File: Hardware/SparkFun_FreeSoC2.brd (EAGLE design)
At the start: 116.8 x 53.3 mm, 109 parts, among them U1 CY8C5888AXI-LP035, U2 MIC5219 5V, U3 MIC5219 3.3V, U4 2A/20V, U7 CY8C5868LTI-LP039, Y1 32.768kHz

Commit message: Revisions from QC check
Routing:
- net 5V: track 212.3 -> 214.7 mm
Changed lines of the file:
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@@
 <wire x1="54.96" y1="34.67" x2="54.96" y2="33.305" width="0.2032" layer="1"/>
 <wire x1="54.96" y1="33.305" x2="55.245" y2="33.02" width="0.2032" layer="1"/>
-<via x="55.245" y="33.02" extent="1-16" drill="0.254"/>
+<via x="55.245" y="33.02" extent="1-16" drill="0.508"/>
 <wire x1="55.245" y1="33.02" x2="59.436" y2="33.02" width="0.2032" layer="16"/>
 <wire x1="59.436" y1="33.02" x2="60.579" y2="34.163" width="0.2032" layer="16"/>
@@
 <contactref element="C9" pad="2"/>
 <wire x1="68.127" y1="33.837" x2="67.691" y2="33.401" width="0.2032" layer="1"/>
-<via x="67.691" y="33.401" extent="1-16" drill="0.254"/>
+<via x="67.691" y="33.401" extent="1-16" drill="0.508"/>
 <via x="67.691" y="17.78" extent="1-16" drill="0.254"/>
 <via x="20.447" y="37.084" extent="1-16" drill="0.254"/>
@@
 <wire x1="60.96" y1="16.891" x2="61.214" y2="16.637" width="0.2032" layer="1"/>
 <wire x1="52.563" y1="34.813" x2="52.578" y2="34.798" width="0.2032" layer="1"/>
-<via x="52.578" y="34.798" extent="1-16" drill="0.254"/>
+<via x="52.578" y="34.798" extent="1-16" drill="0.508"/>
 <wire x1="68.635" y1="19.05" x2="67.945" y2="19.05" width="0.2032" layer="1"/>
 <wire x1="67.945" y1="19.05" x2="67.691" y2="18.796" width="0.2032" layer="1"/>
@@
 <via x="14.605" y="25.781" extent="1-16" drill="0.254"/>
 <wire x1="53.34" y1="17.708" x2="53.34" y2="16.51" width="0.2032" layer="1"/>
-<via x="53.34" y="16.51" extent="1-16" drill="0.254"/>
+<via x="53.34" y="16.51" extent="1-16" drill="0.508"/>
 <wire x1="33.346" y1="37.719" x2="33.346" y2="38.68" width="0.2032" layer="1"/>
 <wire x1="33.346" y1="38.68" x2="33.401" y2="38.735" width="0.2032" layer="1"/>
@@
 <wire x1="27.051" y1="12.065" x2="27.051" y2="5.588" width="1.016" layer="16"/>
 <wire x1="27.051" y1="5.588" x2="55.499" y2="5.588" width="1.016" layer="16"/>
-<wire x1="57.404" y1="6.731" x2="58.42" y2="6.731" width="1.016" layer="16"/>
+<wire x1="56.642" y1="6.731" x2="58.42" y2="6.731" width="1.016" layer="16"/>
 <via x="58.42" y="6.731" extent="1-16" drill="0.508"/>
 <wire x1="58.42" y1="6.731" x2="58.42" y2="2.667" width="1.016" layer="1"/>
@@
 <wire x1="71.81" y1="28.829" x2="71.81" y2="29.155" width="0.2032" layer="1"/>
 <wire x1="71.81" y1="29.155" x2="71.755" y2="29.21" width="0.2032" layer="1"/>
-<wire x1="55.499" y1="5.588" x2="57.404" y2="6.731" width="0" layer="19" extent="16-16"/>
+<wire x1="56.642" y1="6.731" x2="55.499" y2="5.588" width="1.016" layer="16"/>
 </signal>
 <signal name="DEBUG_LED">

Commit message: Fixed silk/part value for target IC
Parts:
- U1: value CY8C5888AXI-LP035 -> CY8C5888AXI-LP096
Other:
- board text added: "CY8C5888AXI-LP096"
- board text removed: "CY8C5888AXI-LP035"
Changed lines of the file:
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@@
 <layer number="56" name="wert" color="7" fill="1" visible="no" active="no"/>
 <layer number="57" name="tCAD" color="7" fill="1" visible="no" active="no"/>
+<layer number="59" name="tCarbon" color="7" fill="1" visible="no" active="no"/>
+<layer number="60" name="bCarbon" color="7" fill="1" visible="no" active="no"/>
 <layer number="90" name="Modules" color="5" fill="1" visible="no" active="no"/>
 <layer number="91" name="Nets" color="2" fill="1" visible="no" active="no"/>
@@
 <layer number="127" name="_tValues" color="7" fill="1" visible="no" active="no"/>
 <layer number="128" name="_bValues" color="7" fill="1" visible="no" active="no"/>
+<layer number="129" name="Mask" color="7" fill="1" visible="no" active="no"/>
 <layer number="131" name="tAdjust" color="7" fill="1" visible="no" active="no"/>
 <layer number="132" name="bAdjust" color="7" fill="1" visible="no" active="no"/>
@@
 <text x="35.56" y="9.652" size="1.524" layer="21" font="vector" ratio="15" align="center-left">PSoC5LP
 Dev Board</text>
-<text x="54.737" y="35.814" size="0.8128" layer="21" font="vector" ratio="15">CY8C5888AXI-LP035</text>
+<text x="54.737" y="35.814" size="0.8128" layer="21" font="vector" ratio="15">CY8C5888AXI-LP096</text>
 <text x="27.813" y="26.543" size="0.8128" layer="21" font="vector" ratio="15">CY8C5868LTI-LP039</text>
 </plain>
@@
 <attribute name="DESIGNER" value="M. Hord" x="46.99" y="-27.94" size="1.778" layer="51"/>
 </element>
-<element name="U1" library="SparkFun-DigitalIC" package="TQFP-100-14X14MM" value="CY8C5888AXI-LP035" x="60.96" y="26.67">
+<element name="U1" library="SparkFun-DigitalIC" package="TQFP-100-14X14MM" value="CY8C5888AXI-LP096" x="60.96" y="26.67">
 <attribute name="PROD_ID" value="IC-12190" x="60.96" y="26.67" size="1.778" layer="27" font="vector" ratio="15" display="off"/>
 </element>

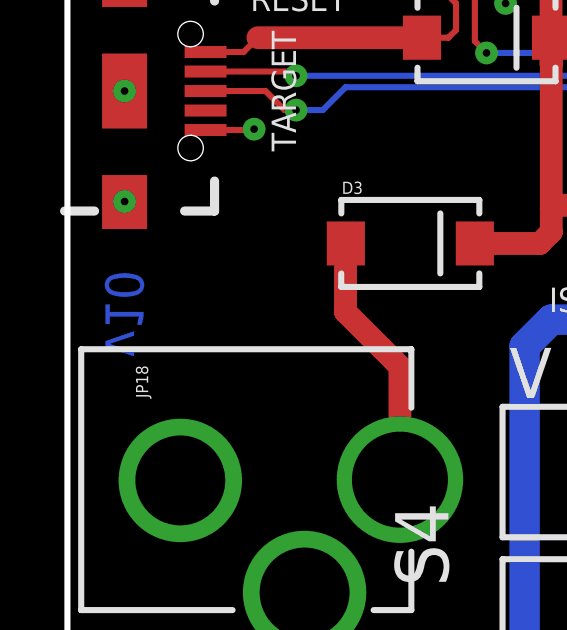
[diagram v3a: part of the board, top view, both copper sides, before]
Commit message: Rev to 11 to fix rev #, layers issue
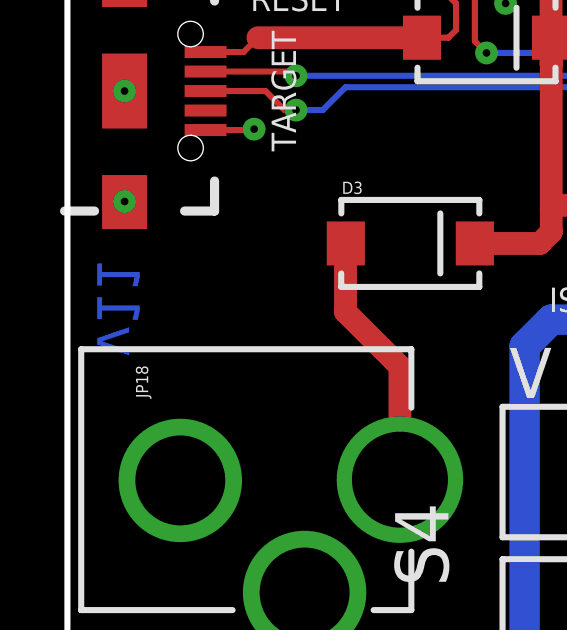
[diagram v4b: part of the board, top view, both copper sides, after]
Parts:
- added U$2: (no value), SparkFun-Aesthetics:CREATIVE_COMMONS
- FRAME1, FRAME2, FRAME3: device SparkFun-Aesthetics:CREATIVE_COMMONS -> SparkFun-Aesthetics:DUMMY
- moved FRAME1 37.8 mm to (-15.2, -15.2)
- moved FRAME2 37.4 mm to (-15.2, -16.5)
- moved FRAME3 37.0 mm to (-15.2, -17.8)
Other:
- board text added: "Mike Hord"
- board text added: "v11"
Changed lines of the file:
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@@
 <layers>
 <layer number="1" name="Top" color="4" fill="1" visible="yes" active="yes"/>
-<layer number="2" name="Route2" color="1" fill="3" visible="no" active="yes"/>
-<layer number="15" name="Route15" color="4" fill="6" visible="no" active="yes"/>
+<layer number="2" name="Route2" color="1" fill="3" visible="yes" active="yes"/>
+<layer number="15" name="Route15" color="4" fill="6" visible="yes" active="yes"/>
 <layer number="16" name="Bottom" color="1" fill="1" visible="yes" active="yes"/>
 <layer number="17" name="Pads" color="2" fill="1" visible="yes" active="yes"/>
@@
 <layer number="23" name="tOrigins" color="15" fill="1" visible="yes" active="yes"/>
 <layer number="24" name="bOrigins" color="15" fill="1" visible="yes" active="yes"/>
-<layer number="25" name="tNames" color="7" fill="1" visible="no" active="yes"/>
-<layer number="26" name="bNames" color="7" fill="1" visible="no" active="yes"/>
-<layer number="27" name="tValues" color="7" fill="1" visible="no" active="yes"/>
-<layer number="28" name="bValues" color="7" fill="1" visible="no" active="yes"/>
-<layer number="29" name="tStop" color="7" fill="3" visible="no" active="yes"/>
-<layer number="30" name="bStop" color="7" fill="6" visible="no" active="yes"/>
-<layer number="31" name="tCream" color="7" fill="4" visible="no" active="yes"/>
-<layer number="32" name="bCream" color="7" fill="5" visible="no" active="yes"/>
-<layer number="39" name="tKeepout" color="4" fill="11" visible="no" active="yes"/>
-<layer number="40" name="bKeepout" color="1" fill="11" visible="no" active="yes"/>
-<layer number="41" name="tRestrict" color="4" fill="10" visible="no" active="yes"/>
-<layer number="42" name="bRestrict" color="1" fill="10" visible="no" active="yes"/>
-<layer number="43" name="vRestrict" color="2" fill="10" visible="no" active="yes"/>
-<layer number="44" name="Drills" color="7" fill="1" visible="no" active="yes"/>
+<layer number="25" name="tNames" color="7" fill="1" visible="yes" active="yes"/>
+<layer number="26" name="bNames" color="7" fill="1" visible="yes" active="yes"/>
+<layer number="27" name="tValues" color="7" fill="1" visible="yes" active="yes"/>
+<layer number="28" name="bValues" color="7" fill="1" visible="yes" active="yes"/>
+<layer number="29" name="tStop" color="7" fill="3" visible="yes" active="yes"/>
+<layer number="30" name="bStop" color="7" fill="6" visible="yes" active="yes"/>
+<layer number="31" name="tCream" color="7" fill="4" visible="yes" active="yes"/>
+<layer number="32" name="bCream" color="7" fill="5" visible="yes" active="yes"/>
+<layer number="39" name="tKeepout" color="4" fill="11" visible="yes" active="yes"/>
+<layer number="40" name="bKeepout" color="1" fill="11" visible="yes" active="yes"/>
+<layer number="41" name="tRestrict" color="4" fill="10" visible="yes" active="yes"/>
+<layer number="42" name="bRestrict" color="1" fill="10" visible="yes" active="yes"/>
+<layer number="43" name="vRestrict" color="2" fill="10" visible="yes" active="yes"/>
+<layer number="44" name="Drills" color="7" fill="1" visible="yes" active="yes"/>
 <layer number="45" name="Holes" color="7" fill="1" visible="yes" active="yes"/>
-<layer number="46" name="Milling" color="3" fill="1" visible="no" active="yes"/>
-<layer number="47" name="Measures" color="7" fill="1" visible="no" active="yes"/>
+<layer number="46" name="Milling" color="3" fill="1" visible="yes" active="yes"/>
+<layer number="47" name="Measures" color="7" fill="1" visible="yes" active="yes"/>
 <layer number="51" name="tDocu" color="6" fill="1" visible="yes" active="yes"/>
 <layer number="52" name="bDocu" color="7" fill="1" visible="no" active="no"/>
@@
 <text x="54.737" y="35.814" size="0.8128" layer="21" font="vector" ratio="15">CY8C5888AXI-LP096</text>
 <text x="27.813" y="26.543" size="0.8128" layer="21" font="vector" ratio="15">CY8C5868LTI-LP039</text>
+<text x="2.413" y="17.272" size="1.4224" layer="16" font="vector" ratio="15" rot="MR270">v11</text>
+<text x="62.23" y="-27.94" size="1.778" layer="51" ratio="15">Mike Hord</text>
 </plain>
 <attributes>
@@
 </autorouter>
 <elements>
-<element name="FRAME1" library="SparkFun-Aesthetics" package="CREATIVE_COMMONS" value="" x="20.32" y="-27.94" smashed="yes">
-<attribute name="VERSION" value="v10" x="1.27" y="13.97" size="1.27" layer="16" font="vector" ratio="15" rot="SMR90"/>
-<attribute name="DESIGNER" value="M. Hord" x="46.99" y="-27.94" size="1.778" layer="51"/>
-</element>
 <element name="U1" library="SparkFun-DigitalIC" package="TQFP-100-14X14MM" value="CY8C5888AXI-LP096" x="60.96" y="26.67">
 <attribute name="PROD_ID" value="IC-12190" x="60.96" y="26.67" size="1.778" layer="27" font="vector" ratio="15" display="off"/>
@@
 <element name="D3" library="SparkFun-DiscreteSemi" package="SMA-DIODE" value="MBRA140" x="11.43" y="17.78">
 <attribute name="PROD_ID" value="DIO-08053" x="-1.27" y="10.16" size="1.778" layer="27" font="vector" ratio="15" display="off"/>
-</element>
-<element name="FRAME2" library="SparkFun-Aesthetics" package="CREATIVE_COMMONS" value="" x="20.32" y="-27.94" smashed="yes">
-<attribute name="VERSION" value="v10" x="49.53" y="-17.78" size="1.27" layer="16" font="vector" ratio="15" rot="SMR0" display="off"/>
-<attribute name="DESIGNER" value="M. Hord" x="46.99" y="-27.94" size="1.778" layer="51" display="off"/>
 </element>
 <element name="JP3" library="SparkFun-Connectors" package="JST-2-PTH" value="M02JST-PTH-2" x="8.89" y="46.99">
@@
 <element name="D4" library="SparkFun-DiscreteSemi" package="SMA-DIODE" value="MBRA140" x="15.621" y="49.149">
 <attribute name="PROD_ID" value="DIO-08053" x="15.621" y="49.149" size="1.778" layer="27" font="vector" ratio="15" display="off"/>
-</element>
-<element name="FRAME3" library="SparkFun-Aesthetics" package="CREATIVE_COMMONS" value="" x="20.32" y="-27.94" smashed="yes">
-<attribute name="VERSION" value="v10" x="49.53" y="-17.78" size="1.27" layer="16" font="vector" ratio="15" rot="SMR0" display="off"/>
-<attribute name="DESIGNER" value="M. Hord" x="46.99" y="-27.94" size="1.778" layer="51" display="off"/>
 </element>
 <element name="U7" library="SparkFun-DigitalIC" package="QFN-68" value="CY8C5868LTI-LP039" x="27.94" y="33.02" rot="R90">
@@
 <element name="SJ6" library="SparkFun-Passives" package="PAD-JUMPER-2-NO_NO_SILK" value="JUMPER-PAD-2-NO" x="43.18" y="43.815" rot="R180"/>
 <element name="SJ7" library="SparkFun-Passives" package="PAD-JUMPER-2-NO_NO_SILK" value="JUMPER-PAD-2-NO" x="43.18" y="41.91" rot="R180"/>
+<element name="FRAME1" library="SparkFun-Aesthetics" package="DUMMY" value="" x="-15.24" y="-15.24">
+<attribute name="VERSION" value="v01" x="-15.24" y="-15.24" size="1.778" layer="27" font="vector" ratio="15" display="off"/>
+<attribute name="DESIGNER" value="Nobody" x="-15.24" y="-15.24" size="1.778" layer="27" font="vector" ratio="15" display="off"/>
+</element>
+<element name="FRAME2" library="SparkFun-Aesthetics" package="DUMMY" value="" x="-15.24" y="-16.51">
+<attribute name="VERSION" value="v01" x="-15.24" y="-16.51" size="1.778" layer="27" font="vector" ratio="15" display="off"/>
+<attribute name="DESIGNER" value="Nobody" x="-15.24" y="-16.51" size="1.778" layer="27" font="vector" ratio="15" display="off"/>
+</element>
+<element name="FRAME3" library="SparkFun-Aesthetics" package="DUMMY" value="" x="-15.24" y="-17.78">
+<attribute name="VERSION" value="v01" x="-15.24" y="-17.78" size="1.778" layer="27" font="vector" ratio="15" display="off"/>
+<attribute name="DESIGNER" value="Nobody" x="-15.24" y="-17.78" size="1.778" layer="27" font="vector" ratio="15" display="off"/>
+</element>
+<element name="U$2" library="SparkFun-Aesthetics" package="CREATIVE_COMMONS" value="" x="35.56" y="-27.94"/>
 </elements>
 <signals>

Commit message: Changed value of DNP caps to DNP
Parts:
- C10, C8: value 470pF -> DNP
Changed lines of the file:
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@@
 <?xml version="1.0" encoding="utf-8"?>
 <!DOCTYPE eagle SYSTEM "eagle.dtd">
-<eagle version="7.1.0">
+<eagle version="7.4.0">
 <drawing>
 <settings>
@@
 <attribute name="PROD_ID" value="VREG-09872" x="24.13" y="24.13" size="1.778" layer="27" font="vector" ratio="15" rot="R270" display="off"/>
 </element>
-<element name="C8" library="SparkFun-Capacitors" package="0603-CAP" value="470pF" x="24.511" y="21.844" rot="R180">
+<element name="C8" library="SparkFun-Capacitors" package="0603-CAP" value="DNP" x="24.511" y="21.844" rot="R180">
 <attribute name="PROD_ID" value="CAP-07884" x="24.511" y="21.844" size="1.778" layer="27" font="vector" ratio="15" rot="R180" display="off"/>
 </element>
-<element name="C10" library="SparkFun-Capacitors" package="0603-CAP" value="470pF" x="24.511" y="14.224" rot="R180">
+<element name="C10" library="SparkFun-Capacitors" package="0603-CAP" value="DNP" x="24.511" y="14.224" rot="R180">
 <attribute name="PROD_ID" value="CAP-07884" x="24.511" y="14.224" size="1.778" layer="27" font="vector" ratio="15" rot="R180" display="off"/>
 </element>
